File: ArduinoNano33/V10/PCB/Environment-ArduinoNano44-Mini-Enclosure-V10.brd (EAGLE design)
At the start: 98.5 x 108 mm, 53 parts, among them IC1 BME680, Q1 310mA/60V/1.6Ω, Q2 310mA/60V/1.6Ω

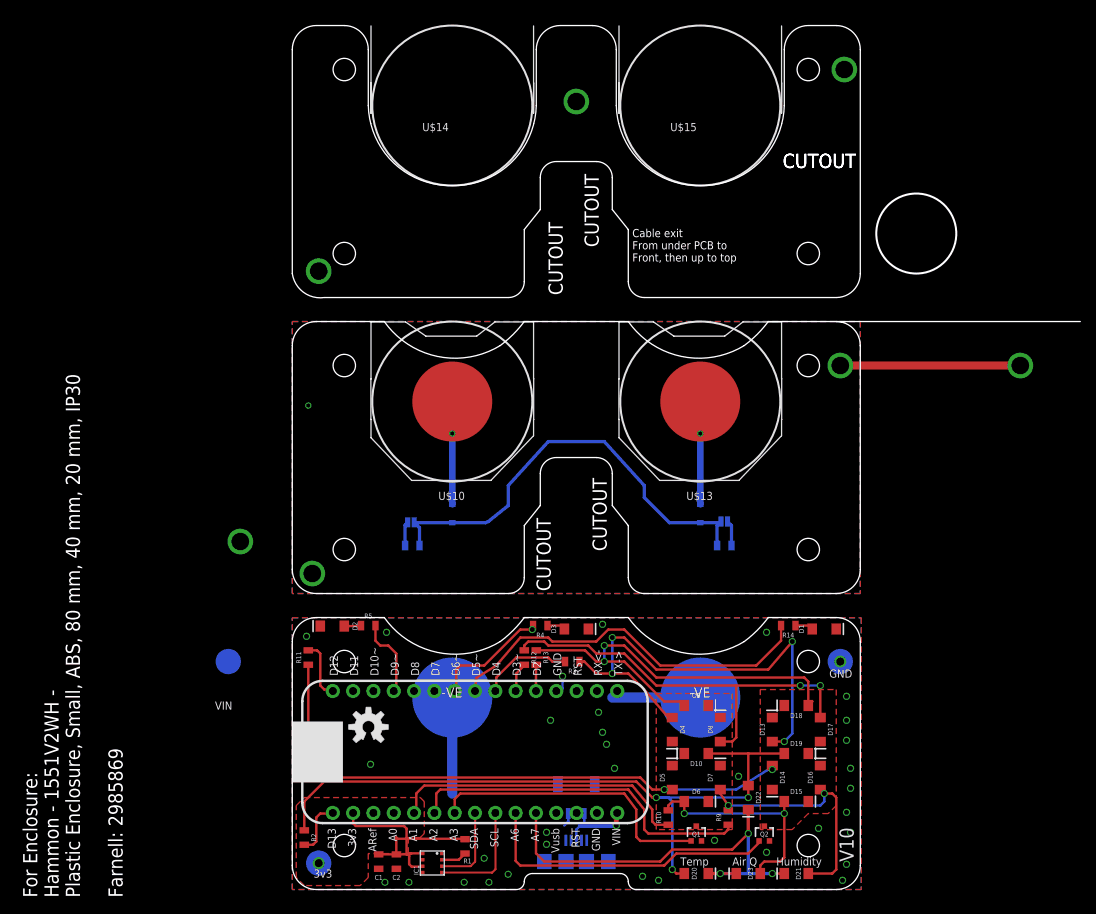
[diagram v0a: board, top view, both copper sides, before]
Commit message: added 7 segment display from LEDs.
Added batteries as internal layers
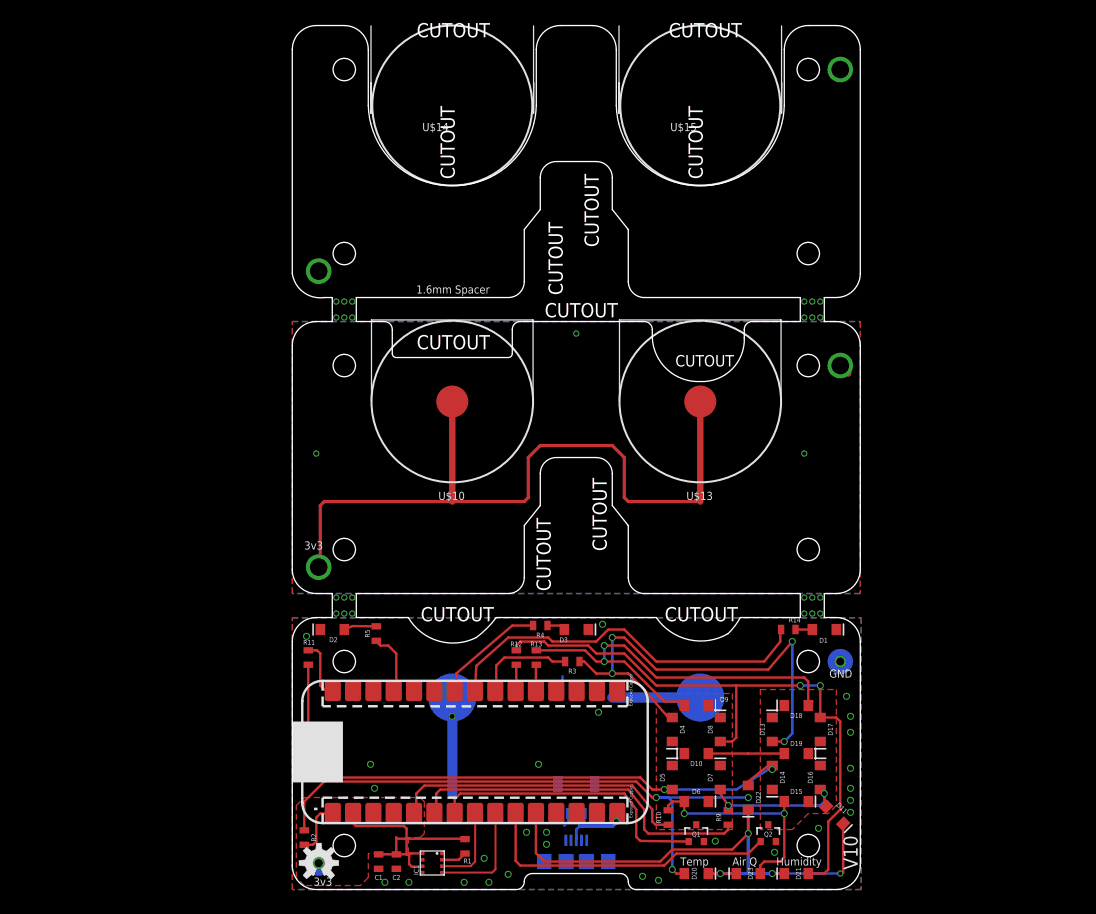
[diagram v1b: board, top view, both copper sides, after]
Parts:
- removed D12: 1A/23V/620mV, SparkFun-DiscreteSemi:SOD-323
- removed JP1, JP3: JUMPER-SMT_2_NC_PASTE_SILK, SparkFun-Jumpers:SMT-JUMPER_2_NC_PASTE_SILK
- removed R7, R8: 0R, SparkFun-Resistors:0805
- D11: value 1A/23V/620mV -> Blue; device SparkFun-DiscreteSemi:SOD-323 -> ThingySticks:LED-1206
- Q1, Q2: value 310mA/60V/1.6Ω -> 5.8A/30V/35mΩ; device SparkFun-DiscreteSemi:SOT323 -> SparkFun-DiscreteSemi:SOT23-3
- U$1: value ARDUINO_33_NANOARDUINO_NANO_33_BLE_SENSE -> ARDUINO_33_NANOARDUINO_NANO_33_BLE_SENSE_SMD; device ThingySticks:ARDUINO_NANO_33 -> ThingySticks:ARDUINO_NANO_33_SMD
- moved D11 60.9 mm to (67.8, 9.30), flipped to the top, turned to 315 degrees
- moved LOGO1 18.1 mm to (3.33, 3.32)
- moved R5 1.41 mm to (10.5, 32.0), turned to 270 degrees
- moved R12 1.00 mm to (28.0, 29.0)
- moved Q2 0.50 mm to (59.5, 7.00)
- moved R14 0.50 mm to (62.0, 32.5)
- moved D2 0.43 mm to (5.00, 32.5)
- moved D3 0.07 mm to (35.5, 32.5)
- moved D1 0.07 mm to (66.5, 32.5)
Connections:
- removed net N$5: D11.A, U$10.+
- removed net N$6: D12.A, U$13.+
- removed net V_BATT: D11.C, D12.C, JP1.2, JP3.1, R7.2, R8.1
- new net NCF_ANTENNA1: U$1.@26
- new net NCF_ANTENNA2: U$1.@25
- net 3.3V: now also U$1.@2, U$10.+, U$13.+; no longer JP1.1, R8.2, U$1.2
- net B: now also D21.A
- net C: now also D11.A; no longer D21.A
- net DIGIT1_SELECT: now also U$1.@7; no longer U$1.7
- net DIGIT2_SELECT: now also U$1.@10; no longer U$1.10
- net DIGIT3: now also D11.C, U$1.@11; no longer U$1.11
- net E: now also D22.A
- net G: no longer D22.A
- net GND: now also U$1.@14, U$1.@19; no longer U$1.14, U$1.19
- net GREEN: now also U$1.@24; no longer U$1.24
- net N$10: now also U$1.@21; no longer U$1.21
- net N$11: now also U$1.@5; no longer U$1.5
- net N$12: now also U$1.@20; no longer U$1.20
- net N$13: now also U$1.@22; no longer U$1.22
- net N$7: now also U$1.@6; no longer U$1.6
- net N$9: now also U$1.@30; no longer U$1.30
- net RED: now also U$1.@23; no longer U$1.23
- net RX: now also U$1.@17; no longer U$1.17
- net SCL: now also U$1.@9; no longer U$1.9
- net SDA: now also U$1.@8; no longer U$1.8
- net TX: now also U$1.@16; no longer U$1.16
- net VIN: now also U$1.@15; no longer JP3.2, R7.1, U$1.15
- net VUSB: now also U$1.@12; no longer U$1.12
- net YELLOW: now also U$1.@27; no longer U$1.27
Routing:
- net 3.3V: track 34.2 -> 123.3 mm, vias 2 -> 3
- net V_BATT: track 55.7 -> 0.00 mm
- net B: track 52.8 -> 78.3 mm
- net GND: track 49.6 -> 28.9 mm, vias 42 -> 35
- net DIGIT3: track 53.0 -> 67.9 mm, vias 3 -> 4
- net N$6: track 12.9 -> 0.00 mm, vias 1 -> 0
- net N$5: track 12.9 -> 0.00 mm, vias 1 -> 0
- net C: track 31.2 -> 18.6 mm
- net G: track 88.4 -> 82.9 mm
- net E: track 73.8 -> 78.0 mm
- net VIN: track 12.9 -> 9.39 mm, vias 2 -> 1
- net N$16: track 2.13 -> 4.09 mm
- net YELLOW: track 9.99 -> 8.19 mm
- net N$13: track 11.6 -> 12.4 mm
- net GREEN: track 14.8 -> 14.1 mm, vias 1 -> 0
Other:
- board size 98.5 x 108 mm -> 71 x 108 mm
- board text added: "1.6mm Spacer"
- board text added: "Battery +VE"
- board text added: "Bettary +VE"
- board text added: "Do not fit batteries when on external power"
- board text removed: "Bettery +VE"
- board text removed: "Do not fit battery when on external power"
- board text removed: "VIN"
